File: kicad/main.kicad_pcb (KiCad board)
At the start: 2 copper layers, 97.8 x 88.9 mm, 47 parts, among them J1 Jack-DC, J2 LCD, J3 Addr, J4 IO~{EN}_{[2..7]}, J5 VIA_A, J6 VIA_B, J7 Data, J8 Control, SW1 Step, SW2 Reset, X1 1 MHz

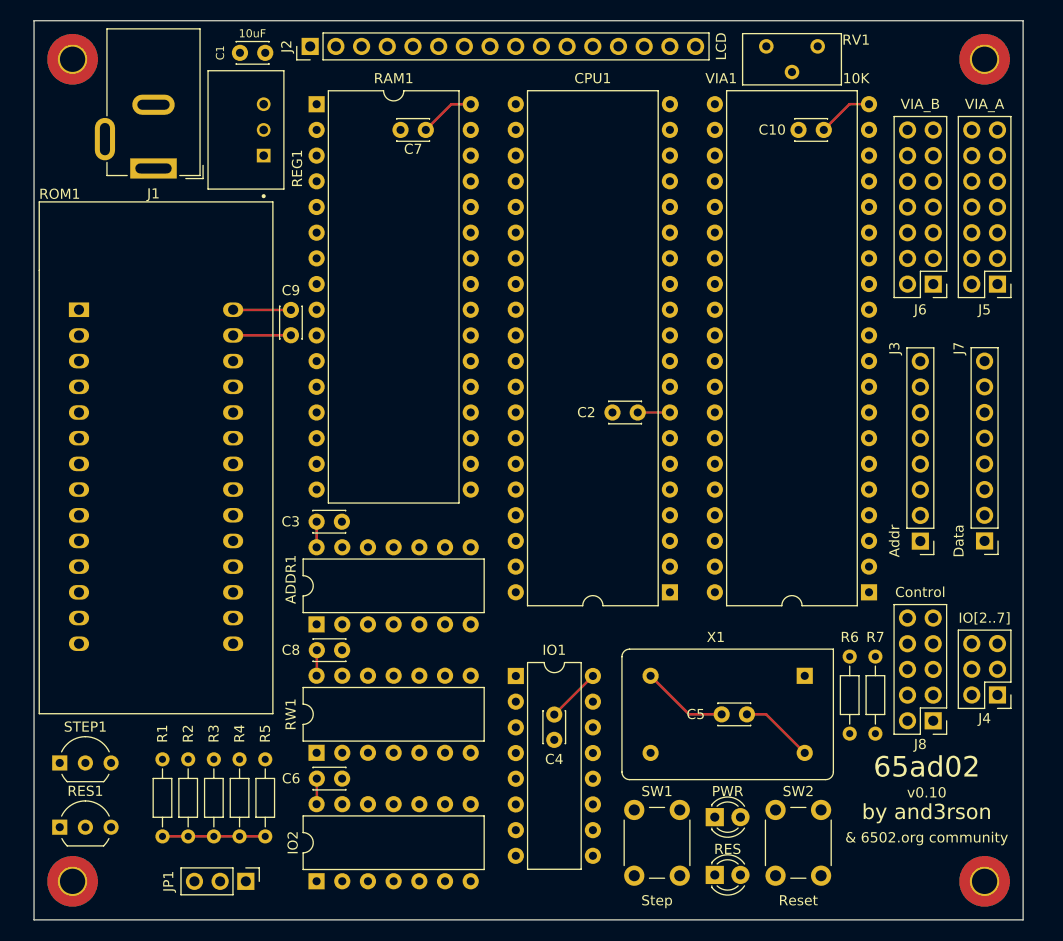
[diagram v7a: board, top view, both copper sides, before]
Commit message: V0.12: (PS/2 & 4-bit LCD with VIA), cleanup kicad libs
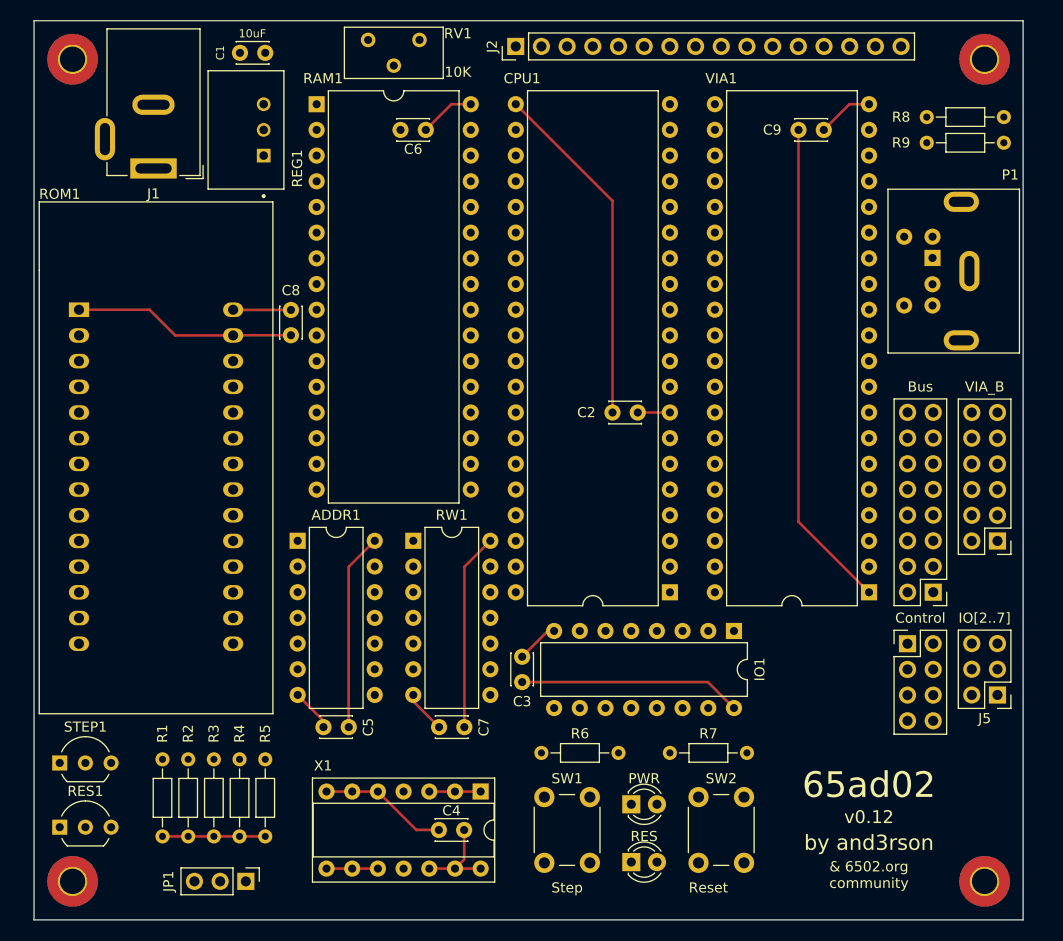
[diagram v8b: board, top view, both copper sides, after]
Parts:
- removed the C6 at (47.6, 92.1)
- removed IO2: 74HC00, Package_DIP:DIP-14_W7.62mm
- removed the J5 at (114.9, 43.2)
- removed J7: Data, Connector_PinHeader_2.54mm:PinHeader_1x08_P2.54mm_Vertical
- removed J8: Control, Connector_PinHeader_2.54mm:PinHeader_2x05_P2.54mm_Vertical
- added J4: VIA_B, Connector_PinHeader_2.54mm:PinHeader_2x06_P2.54mm_Vertical, F.Cu at (114.9, 68.6)
- added P1: Mini-DIN-6, Custom_Footprints:Connector_Mini-DIN_Female_6Pin_2rows, F.Cu at (108.5, 40.6)
- added R8: 1K, Resistor_THT:R_Axial_DIN0204_L3.6mm_D1.6mm_P7.62mm_Horizontal, F.Cu at (108.0, 26.7)
- added R9: 1K, Resistor_THT:R_Axial_DIN0204_L3.6mm_D1.6mm_P7.62mm_Horizontal, F.Cu at (108.0, 29.2)
- J3: value Addr -> Bus; footprint Connector_PinHeader_2.54mm:PinHeader_1x08_P2.54mm_Vertical -> Connector_PinHeader_2.54mm:PinHeader_2x08_P2.54mm_Vertical
- J6: value VIA_B -> Control; footprint Connector_PinHeader_2.54mm:PinHeader_2x07_P2.54mm_Vertical -> Connector_PinHeader_2.54mm:PinHeader_2x04_P2.54mm_Vertical
- X1: value 1 MHz -> 4 MHz; footprint Oscillator:Oscillator_DIP-14 -> Package_DIP:DIP-14_W7.62mm_Socket
- moved RV1 39.4 mm to (57.8, 19.0)
- moved J6 35.6 mm to (106.0, 78.7), turned to 0 degrees
- moved X1 34.0 mm to (63.8, 93.4), turned to -90 degrees
- moved R6 31.9 mm to (69.8, 89.5), turned to 0 degrees
- moved C4 30.2 mm to (59.7, 97.2)
- moved RW1 23.0 mm to (57.2, 68.6), turned to 0 degrees
- moved IO1 22.0 mm to (88.9, 77.5), turned to -90 degrees
- moved C5 20.6 mm to (50.8, 87.0), turned to 180 degrees
- moved J2 20.3 mm to (67.3, 19.7)
- moved C7 16.5 mm to (62.2, 87.0), turned to 180 degrees
- moved R7 15.9 mm to (90.2, 89.5), turned to 180 degrees
- moved SW1 8.98 mm to (70.1, 100.4)
- moved C3 8.81 mm to (67.9, 80.0), turned to -90 degrees
- moved ADDR1 8.47 mm to (45.8, 68.6), turned to 0 degrees
- moved D1 8.35 mm to (78.7, 94.6)
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- renumbered C4 to C3, C5 to C4, C3 to C5, C7 to C6, C8 to C7, C9 to C8, C10 to C9, J4 to J5
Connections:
- CPU1 pad 37: Net-(CPU1-Pad37) -> Ф2
- CPU1 pad 39: Ф2 -> unconnected-(CPU1-Pad39)
- IO1 pad 14: VIA~{EN} -> unconnected-(IO1-Pad14)
- IO1 pad 15: Net-(IO2-Pad1) -> VIA~{EN}
- J2 pad 10: D_{3} -> unconnected-(J2-Pad10)
- J2 pad 11: D_{4} -> PA_{0}
- J2 pad 12: D_{5} -> PA_{1}
- J2 pad 13: D_{6} -> PA_{2}
- J2 pad 14: D_{7} -> PA_{3}
- J2 pad 4: A_{0} -> PA_{6}
- J2 pad 5: R~{W} -> PA_{5}
- J2 pad 6: LCDEN -> PA_{4}
- J2 pad 7: D_{0} -> unconnected-(J2-Pad7)
- J2 pad 8: D_{1} -> unconnected-(J2-Pad8)
- J2 pad 9: D_{2} -> unconnected-(J2-Pad9)
- J6 pad 3: Net-(J6-Pad3) -> R~{W}
- J6 pad 4: Net-(J6-Pad4) -> ~{RD}
- J6 pad 5: Net-(J6-Pad5) -> ~{WD}
- J6 pad 6: Net-(J6-Pad6) -> Ф2
- J6 pad 7: Net-(J6-Pad7) -> ~{IRQ}
- J6 pad 8: Net-(J6-Pad8) -> ~{RES}
- JP1 pad 2: Net-(CPU1-Pad37) -> Ф2
- VIA1 pad 10: Net-(J6-Pad3) -> Net-(J4-Pad3)
- VIA1 pad 11: Net-(J6-Pad4) -> Net-(J4-Pad4)
- VIA1 pad 12: Net-(J6-Pad5) -> Net-(J4-Pad5)
- VIA1 pad 13: Net-(J6-Pad6) -> Net-(J4-Pad6)
- VIA1 pad 14: Net-(J6-Pad7) -> Net-(J4-Pad7)
- VIA1 pad 15: Net-(J6-Pad8) -> Net-(J4-Pad8)
- VIA1 pad 16: Net-(J6-Pad9) -> Net-(J4-Pad9)
- VIA1 pad 17: Net-(J6-Pad10) -> Net-(J4-Pad10)
- VIA1 pad 18: Net-(J6-Pad11) -> Net-(J4-Pad11)
- VIA1 pad 19: Net-(J6-Pad12) -> Net-(J4-Pad12)
- VIA1 pad 2: Net-(J5-Pad3) -> PA_{0}
- VIA1 pad 3: Net-(J5-Pad4) -> PA_{1}
- VIA1 pad 39: Net-(J5-Pad12) -> unconnected-(VIA1-Pad39)
- VIA1 pad 4: Net-(J5-Pad5) -> PA_{2}
- VIA1 pad 40: Net-(J5-Pad11) -> CA1
- VIA1 pad 5: Net-(J5-Pad6) -> PA_{3}
- VIA1 pad 6: Net-(J5-Pad7) -> PA_{4}
- VIA1 pad 7: Net-(J5-Pad8) -> PA_{5}
- VIA1 pad 8: Net-(J5-Pad9) -> PA_{6}
- VIA1 pad 9: Net-(J5-Pad10) -> PA_{7}
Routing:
- net GND: track 14.3 -> 130.4 mm
- net +5V: track 50.4 -> 100.3 mm
- net unconnected-(X1-Pad1): track 0.00 -> 5.08 mm
- net CLK: track 0.00 -> 5.08 mm
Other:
- board text added: "v0.12"
- board text removed: "Addr"
- board text removed: "Control"
- board text removed: "Data"
- board text removed: "VIA_A"
- board text removed: "VIA_B"
- board text removed: "v0.10"
